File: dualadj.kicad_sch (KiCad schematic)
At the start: 12 parts, among them J8 Conn_01x02_Female, J9 Conn_01x02_Female, U8 LM317L_TO92, U9 LM337L_TO92

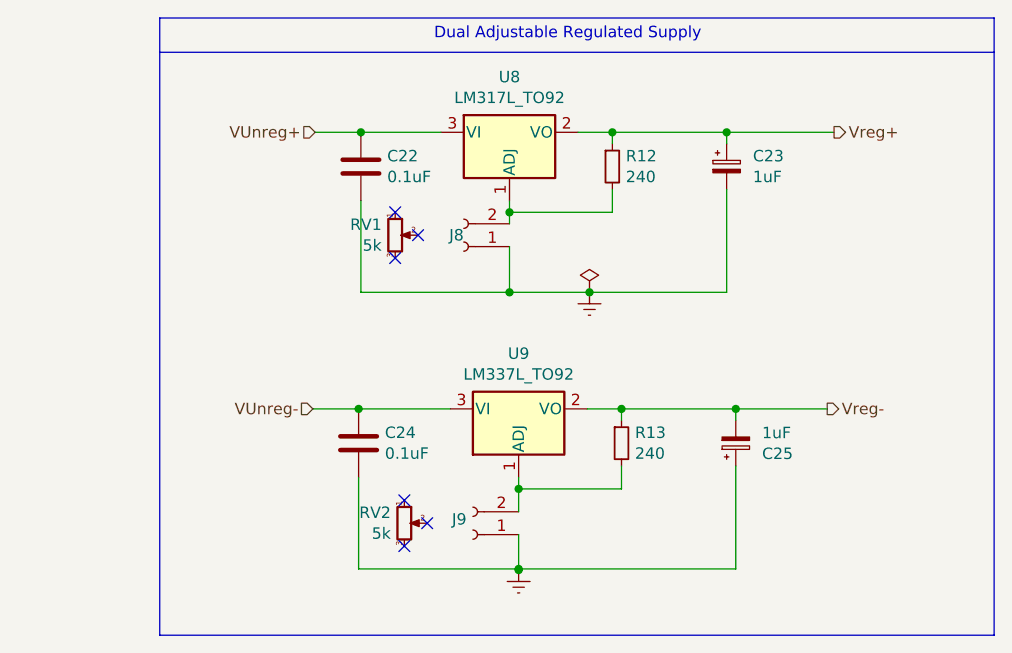
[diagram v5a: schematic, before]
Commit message: Updated improved board for all SMD
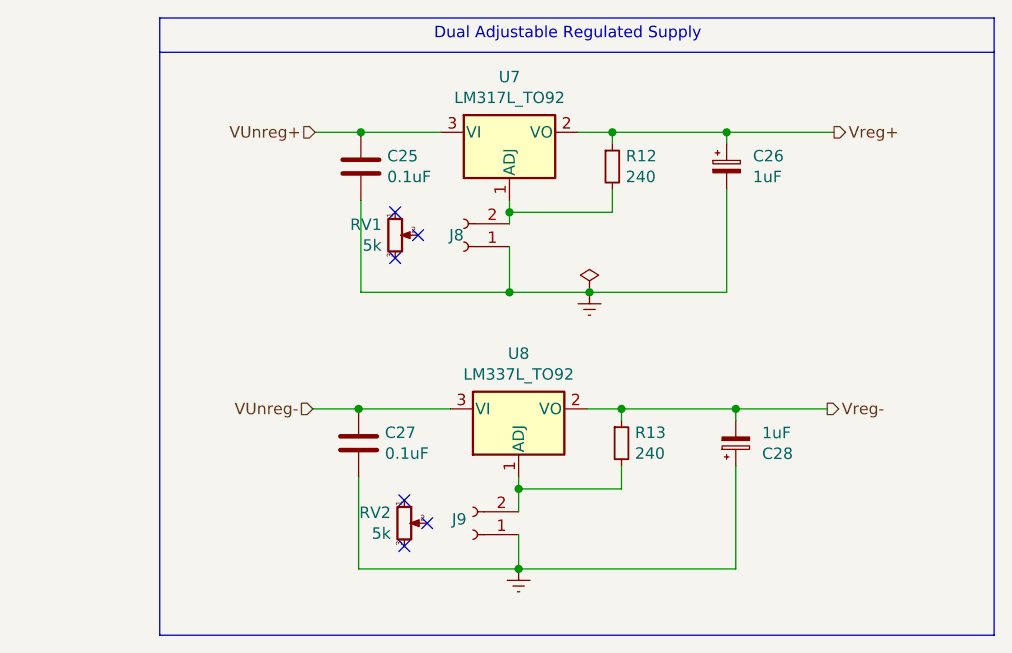
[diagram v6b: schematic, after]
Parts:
- renumbered C22 to C25, C23 to C26, C24 to C27, C25 to C28, U8 to U7, U9 to U8
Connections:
- net GNDREF: now also C27.2, C28.1, J9.1 (Pin_1)
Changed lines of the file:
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@@
   (junction (at 136.652 81.28) (diameter 0) (color 0 0 0 0)
   )
+  (junction (at 120.142 72.39) (diameter 0) (color 0 0 0 0)
+  )
+  (junction (at 136.652 90.17) (diameter 0) (color 0 0 0 0)
+  )
+  (junction (at 149.098 103.124) (diameter 0) (color 0 0 0 0)
+  )
   (junction (at 137.668 120.904) (diameter 0) (color 0 0 0 0)
   )
-  (junction (at 120.142 72.39) (diameter 0) (color 0 0 0 0)
-  )
-  (junction (at 136.652 90.17) (diameter 0) (color 0 0 0 0)
-  )
-  (junction (at 149.098 103.124) (diameter 0) (color 0 0 0 0)
-  )
   (junction (at 137.668 112.014) (diameter 0) (color 0 0 0 0)
-  )
-  (junction (at 137.668 121.031) (diameter 0) (color 0 0 0 0)
   )
   (junction (at 160.782 72.39) (diameter 0) (color 0 0 0 0)
@@
     (stroke (width 0) (type default) (color 0 0 0 0))
   )
+  (wire (pts (xy 137.668 120.904) (xy 161.798 120.904))
+    (stroke (width 0) (type default) (color 0 0 0 0))
+  )
+  (wire (pts (xy 149.098 104.394) (xy 149.098 103.124))
+    (stroke (width 0) (type default) (color 0 0 0 0))
+  )
+  (wire (pts (xy 145.288 103.124) (xy 149.098 103.124))
+    (stroke (width 0) (type default) (color 0 0 0 0))
+  )
   (wire (pts (xy 119.888 120.904) (xy 137.668 120.904))
-    (stroke (width 0) (type default) (color 0 0 0 0))
-  )
-  (wire (pts (xy 149.098 104.394) (xy 149.098 103.124))
-    (stroke (width 0) (type default) (color 0 0 0 0))
-  )
-  (wire (pts (xy 145.288 103.124) (xy 149.098 103.124))
-    (stroke (width 0) (type default) (color 0 0 0 0))
-  )
-  (wire (pts (xy 137.668 120.904) (xy 161.798 120.904))
     (stroke (width 0) (type default) (color 0 0 0 0))
   )
@@
   (symbol (lib_id "Device:C") (at 120.142 76.2 0) (unit 1)
     (in_bom yes) (on_board yes)
-    (property "Reference" "C22" (id 0) (at 123.063 75.0316 0)
+    (property "Reference" "C25" (id 0) (at 123.063 75.0316 0)
       (effects (font (size 1.27 1.27)) (justify left))
     )
@@
   (symbol (lib_id "Device:C_Polarized_Small") (at 161.798 106.934 0) (mirror x) (unit 1)
     (in_bom yes) (on_board yes)
-    (property "Reference" "C25" (id 0) (at 164.719 108.1024 0)
+    (property "Reference" "C28" (id 0) (at 164.719 108.1024 0)
       (effects (font (size 1.27 1.27)) (justify left))
     )
@@
   (symbol (lib_id "power:PWR_FLAG") (at 145.542 90.17 0) (unit 1)
     (in_bom yes) (on_board yes)
-    (property "Reference" "#FLG07" (id 0) (at 145.542 88.265 0)
+    (property "Reference" "#FLG02" (id 0) (at 145.542 88.265 0)
       (effects (font (size 1.27 1.27)) hide)
     )
@@
   (symbol (lib_id "Regulator_Linear:LM317L_TO92") (at 136.652 72.39 0) (unit 1)
     (in_bom yes) (on_board yes)
-    (property "Reference" "U8" (id 0) (at 136.652 66.2432 0))
+    (property "Reference" "U7" (id 0) (at 136.652 66.2432 0))
     (property "Value" "LM317L_TO92" (id 1) (at 136.652 68.5546 0))
     (property "Footprint" "Package_TO_SOT_SMD:SOT-223-3_TabPin2" (id 2) (at 136.652 66.675 0)
@@
   (symbol (lib_id "Device:C") (at 119.888 106.934 0) (unit 1)
     (in_bom yes) (on_board yes)
-    (property "Reference" "C24" (id 0) (at 122.809 105.7656 0)
+    (property "Reference" "C27" (id 0) (at 122.809 105.7656 0)
       (effects (font (size 1.27 1.27)) (justify left))
     )
@@
   (symbol (lib_id "Regulator_Linear:LM337L_TO92") (at 137.668 103.124 0) (mirror x) (unit 1)
     (in_bom yes) (on_board yes)
-    (property "Reference" "U9" (id 0) (at 137.668 96.9772 0))
+    (property "Reference" "U8" (id 0) (at 137.668 96.9772 0))
     (property "Value" "LM337L_TO92" (id 1) (at 137.668 99.2886 0))
     (property "Footprint" "Package_TO_SOT_SMD:SOT-223-3_TabPin2" (id 2) (at 137.668 98.044 0)
@@
     (pin "3")
   )
-  (symbol (lib_id "power:GNDREF") (at 137.668 121.031 0) (unit 1)
+  (symbol (lib_id "power:GNDREF") (at 137.668 120.904 0) (unit 1)
     (in_bom yes) (on_board yes) (fields_autoplaced)
-    (property "Reference" "#PWR0102" (id 0) (at 137.668 127.381 0)
-      (effects (font (size 1.27 1.27)) hide)
-    )
-    (property "Value" "GNDREF" (id 1) (at 137.668 125.4744 0)
-      (effects (font (size 1.27 1.27)) hide)
-    )
-    (property "Footprint" "" (id 2) (at 137.668 121.031 0)
-      (effects (font (size 1.27 1.27)) hide)
-    )
-    (property "Datasheet" "" (id 3) (at 137.668 121.031 0)
+    (property "Reference" "#PWR028" (id 0) (at 137.668 127.254 0)
+      (effects (font (size 1.27 1.27)) hide)
+    )
+    (property "Value" "GNDREF" (id 1) (at 137.668 125.3474 0)
+      (effects (font (size 1.27 1.27)) hide)
+    )
+    (property "Footprint" "" (id 2) (at 137.668 120.904 0)
+      (effects (font (size 1.27 1.27)) hide)
+    )
+    (property "Datasheet" "" (id 3) (at 137.668 120.904 0)
       (effects (font (size 1.27 1.27)) hide)
     )
@@
   (symbol (lib_id "power:GNDREF") (at 145.542 90.17 0) (unit 1)
     (in_bom yes) (on_board yes) (fields_autoplaced)
-    (property "Reference" "#PWR0103" (id 0) (at 145.542 96.52 0)
+    (property "Reference" "#PWR027" (id 0) (at 145.542 96.52 0)
       (effects (font (size 1.27 1.27)) hide)
     )
@@
   (symbol (lib_id "Device:C_Polarized_Small") (at 160.782 76.2 0) (unit 1)
     (in_bom yes) (on_board yes)
-    (property "Reference" "C23" (id 0) (at 163.703 75.0316 0)
-      (effects (font (size 1.27 1.27)) (justify left))
-    )
+    (property "Reference" "C26" (id 0) (at 163.703 75.0316 0)
+      (effects (font (size 1.27 1.27)) (justify left))
+    )

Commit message: added new op amps and used automated traces due to complexity
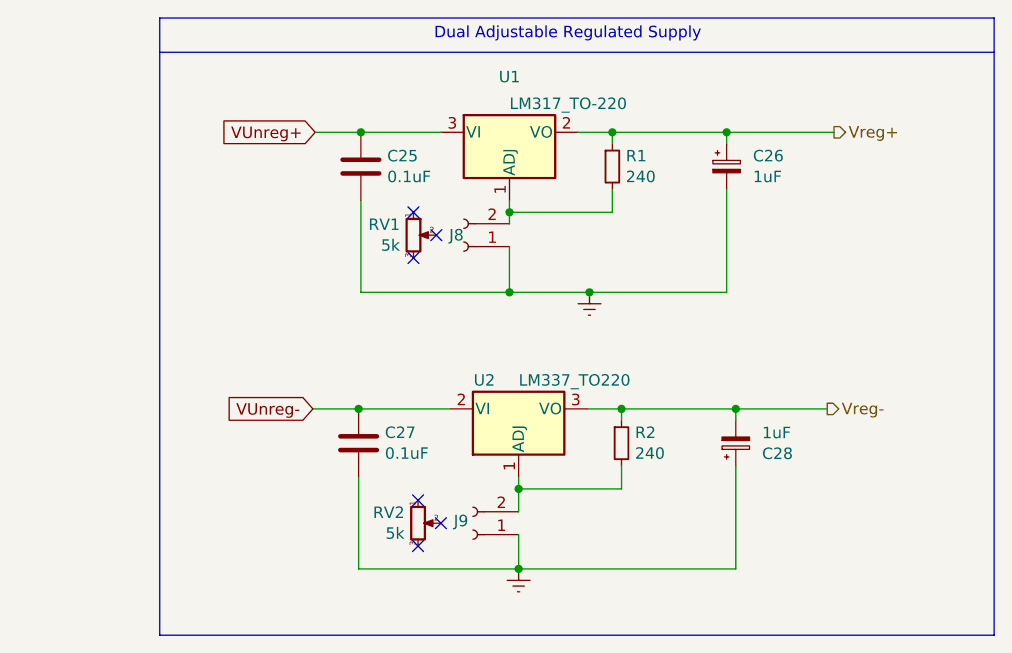
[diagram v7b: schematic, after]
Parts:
- U1: renamed from U7; value LM317L_TO92 -> LM317_TO-220; symbol Regulator_Linear:LM317L_TO92 -> Regulator_Linear:LM317_TO-220; Availability on order -> (none)
- U2: renamed from U8; value LM337L_TO92 -> LM337_TO220; symbol Regulator_Linear:LM337L_TO92 -> Regulator_Linear:LM337_TO220; Availability on order -> (none)
- renumbered R12 to R1, R13 to R2
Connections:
- net VUnreg-: now also U2.2 (VI); no longer U2.3 (VI)
- net Vreg-: now also U2.3 (VO); no longer U2.2 (VO)
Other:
- moved on the sheet: RV1, RV2
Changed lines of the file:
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@@
   (junction (at 145.542 90.17) (diameter 0) (color 0 0 0 0)
   )
-  (no_connect (at 126.492 83.82))
-  (no_connect (at 123.952 86.36))
-  (no_connect (at 127.508 115.824))
-  (no_connect (at 123.952 81.28))
-  (no_connect (at 124.968 118.364))
-  (no_connect (at 124.968 113.284))
+  (no_connect (at 128.524 83.82))
+  (no_connect (at 125.984 86.36))
+  (no_connect (at 129.032 115.824))
+  (no_connect (at 125.984 81.28))
+  (no_connect (at 126.492 118.364))
+  (no_connect (at 126.492 113.284))
   (wire (pts (xy 160.782 90.17) (xy 160.782 78.74))
     (stroke (width 0) (type default) (color 0 0 0 0))
@@
     (effects (font (size 1.27 1.27)) (justify left bottom))
   )
+  (global_label "VUnreg+" (shape input) (at 115.062 72.39 180) (fields_autoplaced)
+    (effects (font (size 1.27 1.27)) (justify right))
+    (property "Intersheet References" "${INTERSHEET_REFS}" (id 0) (at 104.5735 72.3106 0)
+      (effects (font (size 1.27 1.27)) (justify right))
+    )
+  )
+  (global_label "VUnreg-" (shape input) (at 114.808 103.124 180) (fields_autoplaced)
+    (effects (font (size 1.27 1.27)) (justify right))
+    (property "Intersheet References" "${INTERSHEET_REFS}" (id 0) (at 104.3195 103.0446 0)
+      (effects (font (size 1.27 1.27)) (justify right))
+    )
+  )
   (hierarchical_label "Vreg+" (shape output) (at 172.72 72.39 0)
     (effects (font (size 1.27 1.27)) (justify left))
   )
-  (hierarchical_label "VUnreg-" (shape input) (at 114.808 103.124 180)
-    (effects (font (size 1.27 1.27)) (justify right))
-  )
   (hierarchical_label "Vreg-" (shape output) (at 171.958 103.124 0)
     (effects (font (size 1.27 1.27)) (justify left))
   )
-  (hierarchical_label "VUnreg+" (shape input) (at 115.062 72.39 180)
-    (effects (font (size 1.27 1.27)) (justify right))
-  )
   (symbol (lib_id "Device:C") (at 120.142 76.2 0) (unit 1)
     (in_bom yes) (on_board yes)
@@
   )
   (symbol (lib_id "Connector:Conn_01x02_Female") (at 132.588 117.094 180) (unit 1)
-    (in_bom yes) (on_board yes) (fields_autoplaced)
-    (property "Reference" "J9" (id 0) (at 131.8768 115.3902 0)
+    (in_bom yes) (on_board yes)
+    (property "Reference" "J9" (id 0) (at 132.08 115.57 0)
       (effects (font (size 1.27 1.27)) (justify left))
     )
@@
   (symbol (lib_id "Device:R_Small") (at 148.082 76.2 0) (unit 1)
     (in_bom yes) (on_board yes)
-    (property "Reference" "R12" (id 0) (at 149.5806 75.0316 0)
+    (property "Reference" "R1" (id 0) (at 149.5806 75.0316 0)
       (effects (font (size 1.27 1.27)) (justify left))
     )
@@
     (pin "2")
   )
-  (symbol (lib_id "power:PWR_FLAG") (at 145.542 90.17 0) (unit 1)
-    (in_bom yes) (on_board yes)
-    (property "Reference" "#FLG02" (id 0) (at 145.542 88.265 0)
-      (effects (font (size 1.27 1.27)) hide)
-    )
-    (property "Value" "PWR_FLAG" (id 1) (at 145.542 85.7758 0)
-      (effects (font (size 1.27 1.27)) hide)
-    )
-    (property "Footprint" "" (id 2) (at 145.542 90.17 0)
-      (effects (font (size 1.27 1.27)) hide)
-    )
-    (property "Datasheet" "~" (id 3) (at 145.542 90.17 0)
-      (effects (font (size 1.27 1.27)) hide)
-    )
-    (pin "1")
-  )
-  (symbol (lib_id "Regulator_Linear:LM317L_TO92") (at 136.652 72.39 0) (unit 1)
-    (in_bom yes) (on_board yes)
-    (property "Reference" "U7" (id 0) (at 136.652 66.2432 0))
-    (property "Value" "LM317L_TO92" (id 1) (at 136.652 68.5546 0))
-    (property "Footprint" "Package_TO_SOT_SMD:SOT-223-3_TabPin2" (id 2) (at 136.652 66.675 0)
+  (symbol (lib_id "Regulator_Linear:LM317_TO-220") (at 136.652 72.39 0) (unit 1)
+    (in_bom yes) (on_board yes)
+    (property "Reference" "U1" (id 0) (at 136.652 66.2432 0))
+    (property "Value" "LM317_TO-220" (id 1) (at 136.652 69.215 0)
+      (effects (font (size 1.27 1.27)) (justify left))
+    )
+    (property "Footprint" "Package_TO_SOT_SMD:SOT-223-3_TabPin2" (id 2) (at 136.652 66.04 0)
       (effects (font (size 1.27 1.27) italic) hide)
     )
-    (property "Datasheet" "http://www.ti.com/lit/ds/snvs775k/snvs775k.pdf" (id 3) (at 136.652 72.39 0)
-      (effects (font (size 1.27 1.27)) hide)
-    )
-    (property "Availability" "on order" (id 4) (at 136.652 72.39 0)
+    (property "Datasheet" "http://www.ti.com/lit/ds/symlink/lm317.pdf" (id 3) (at 136.652 72.39 0)
       (effects (font (size 1.27 1.27)) hide)
     )
@@
     (pin "3")
   )
-  (symbol (lib_id "minipowersupply-rescue:R_POT_Small-Device") (at 124.968 115.824 0) (unit 1)
-    (in_bom yes) (on_board yes)
-    (property "Reference" "RV2" (id 0) (at 123.4694 114.6556 0)
-      (effects (font (size 1.27 1.27)) (justify right))
-    )
-    (property "Value" "5k" (id 1) (at 123.4694 116.967 0)
-      (effects (font (size 1.27 1.27)) (justify right))
-    )
-    (property "Footprint" "" (id 2) (at 124.968 115.824 0)
-      (effects (font (size 1.27 1.27)) hide)
-    )
-    (property "Datasheet" "~" (id 3) (at 124.968 115.824 0)
-      (effects (font (size 1.27 1.27)) hide)
-    )
-    (property "Availability" "On ORder" (id 4) (at 124.968 115.824 0)
+  (symbol (lib_id "minipowersupply-rescue:R_POT_Small-Device") (at 126.492 115.824 0) (unit 1)
+    (in_bom yes) (on_board no)
+    (property "Reference" "RV2" (id 0) (at 124.9934 114.6556 0)
+      (effects (font (size 1.27 1.27)) (justify right))
+    )
+    (property "Value" "5k" (id 1) (at 124.9934 116.967 0)
+      (effects (font (size 1.27 1.27)) (justify right))
+    )
+    (property "Footprint" "" (id 2) (at 126.492 115.824 0)
+      (effects (font (size 1.27 1.27)) hide)
+    )
+    (property "Datasheet" "~" (id 3) (at 126.492 115.824 0)
+      (effects (font (size 1.27 1.27)) hide)
+    )
+    (property "Availability" "On ORder" (id 4) (at 126.492 115.824 0)
       (effects (font (size 1.27 1.27)) hide)
     )
@@
     (pin "2")
   )
-  (symbol (lib_id "Regulator_Linear:LM337L_TO92") (at 137.668 103.124 0) (mirror x) (unit 1)
-    (in_bom yes) (on_board yes)
-    (property "Reference" "U8" (id 0) (at 137.668 96.9772 0))
-    (property "Value" "LM337L_TO92" (id 1) (at 137.668 99.2886 0))
+  (symbol (lib_id "Regulator_Linear:LM337_TO220") (at 137.668 103.124 0) (mirror x) (unit 1)
+    (in_bom yes) (on_board yes)
+    (property "Reference" "U2" (id 0) (at 133.858 99.949 0))
+    (property "Value" "LM337_TO220" (id 1) (at 137.668 99.949 0)
+      (effects (font (size 1.27 1.27)) (justify left))
+    )
     (property "Footprint" "Package_TO_SOT_SMD:SOT-223-3_TabPin2" (id 2) (at 137.668 98.044 0)
       (effects (font (size 1.27 1.27) italic) hide)
     )
-    (property "Datasheet" "http://www.ti.com/lit/ds/symlink/lm337l.pdf" (id 3) (at 137.668 103.124 0)
-      (effects (font (size 1.27 1.27)) hide)
-    )
-    (property "Availability" "on order" (id 4) (at 137.668 103.124 0)
+    (property "Datasheet" "http://www.ti.com/lit/ds/symlink/lm337-n.pdf" (id 3) (at 137.668 103.124 0)
       (effects (font (size 1.27 1.27)) hide)
     )
@@
   (symbol (lib_id "Device:R_Small") (at 149.098 106.934 0) (unit 1)
     (in_bom yes) (on_board yes)
-    (property "Reference" "R13" (id 0) (at 150.5966 105.7656 0)
+    (property "Reference" "R2" (id 0) (at 150.5966 105.7656 0)
       (effects (font (size 1.27 1.27)) (justify left))
     )
@@
     (pin "2")
   )
-  (symbol (lib_id "minipowersupply-rescue:R_POT_Small-Device") (at 123.952 83.82 0) (unit 1)
-    (in_bom yes) (on_board yes)
-    (property "Reference" "RV1" (id 0) (at 122.4534 82.6516 0)
-      (effects (font (size 1.27 1.27)) (justify right))
-    )
-    (property "Value" "5k" (id 1) (at 122.4534 84.963 0)
-      (effects (font (size 1.27 1.27)) (justify right))
-    )
-    (property "Footprint" "" (id 2) (at 123.952 83.82 0)
-      (effects (font (size 1.27 1.27)) hide)
-    )
-    (property "Datasheet" "~" (id 3) (at 123.952 83.82 0)
-      (effects (font (size 1.27 1.27)) hide)
-    )
-    (property "Availability" "On ORder" (id 4) (at 123.952 83.82 0)
-      (effects (font (size 1.27 1.27)) hide)
-    )
+  (symbol (lib_id "minipowersupply-rescue:R_POT_Small-Device") (at 125.984 83.82 0) (unit 1)
+    (in_bom yes) (on_board no)
+    (property "Reference" "RV1" (id 0) (at 124.4854 82.6516 0)
+      (effects (font (size 1.27 1.27)) (justify right))
+    )
+    (property "Value" "5k" (id 1) (at 124.4854 84.963 0)
+      (effects (font (size 1.27 1.27)) (justify right))
+    )
+    (property "Footprint" "" (id 2) (at 125.984 83.82 0)
+      (effects (font (size 1.27 1.27)) hide)
+    )
+    (property "Datasheet" "~" (id 3) (at 125.984 83.82 0)
+      (effects (font (size 1.27 1.27)) hide)
+    )
+    (property "Availability" "On ORder" (id 4) (at 125.984 83.82 0)
+      (effects (font (size 1.27 1.27)) hide)
+    )
